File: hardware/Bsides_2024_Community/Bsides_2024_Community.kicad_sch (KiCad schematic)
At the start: 44 parts, among them J1 Add_On, J2 Battery, J3 Battery, J4 OLED, J5 Conn_01x05, J6 Conn_01x05, P1 USB_C_Plug_USB2.0, Q1 DMG3415U-7, SW1 ON, SW2 RESET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

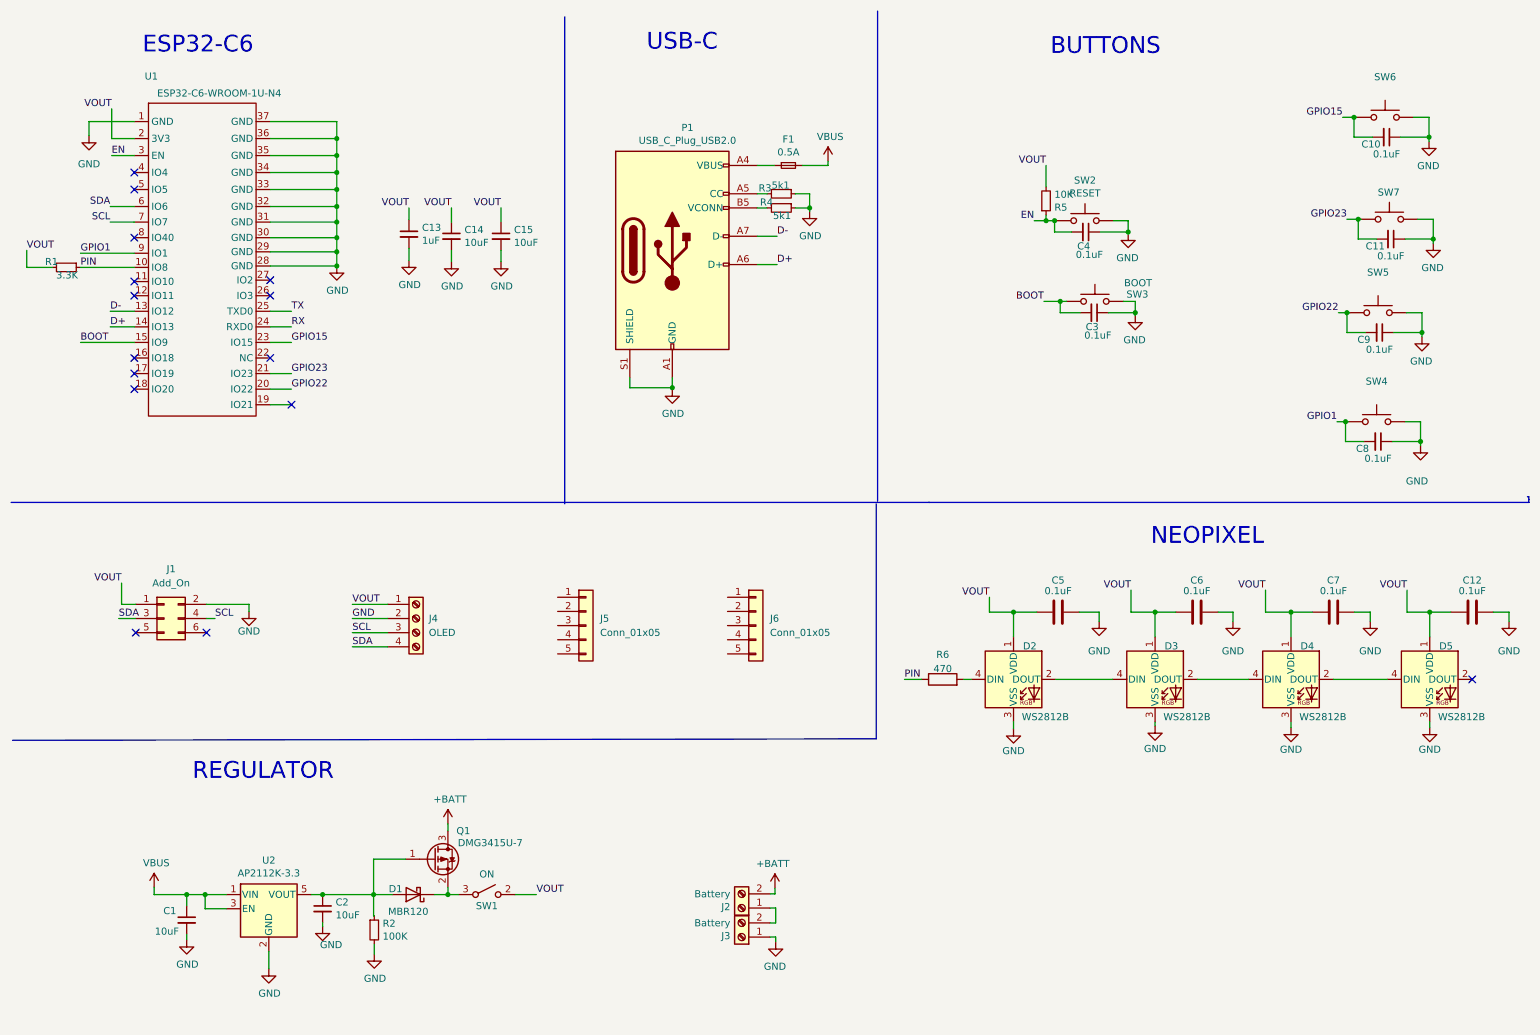
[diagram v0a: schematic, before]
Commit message: Revert "Merge branch 'main' of https://github.com/ElectronicCats/badge-bsides-cdmx-2024"
This reverts commit 844f9cf1141b02d246949023f3a5d84c3d1d6870, reversing
changes made to df45190e2e7c4c17babbd6f5b24a18277498f0c6.
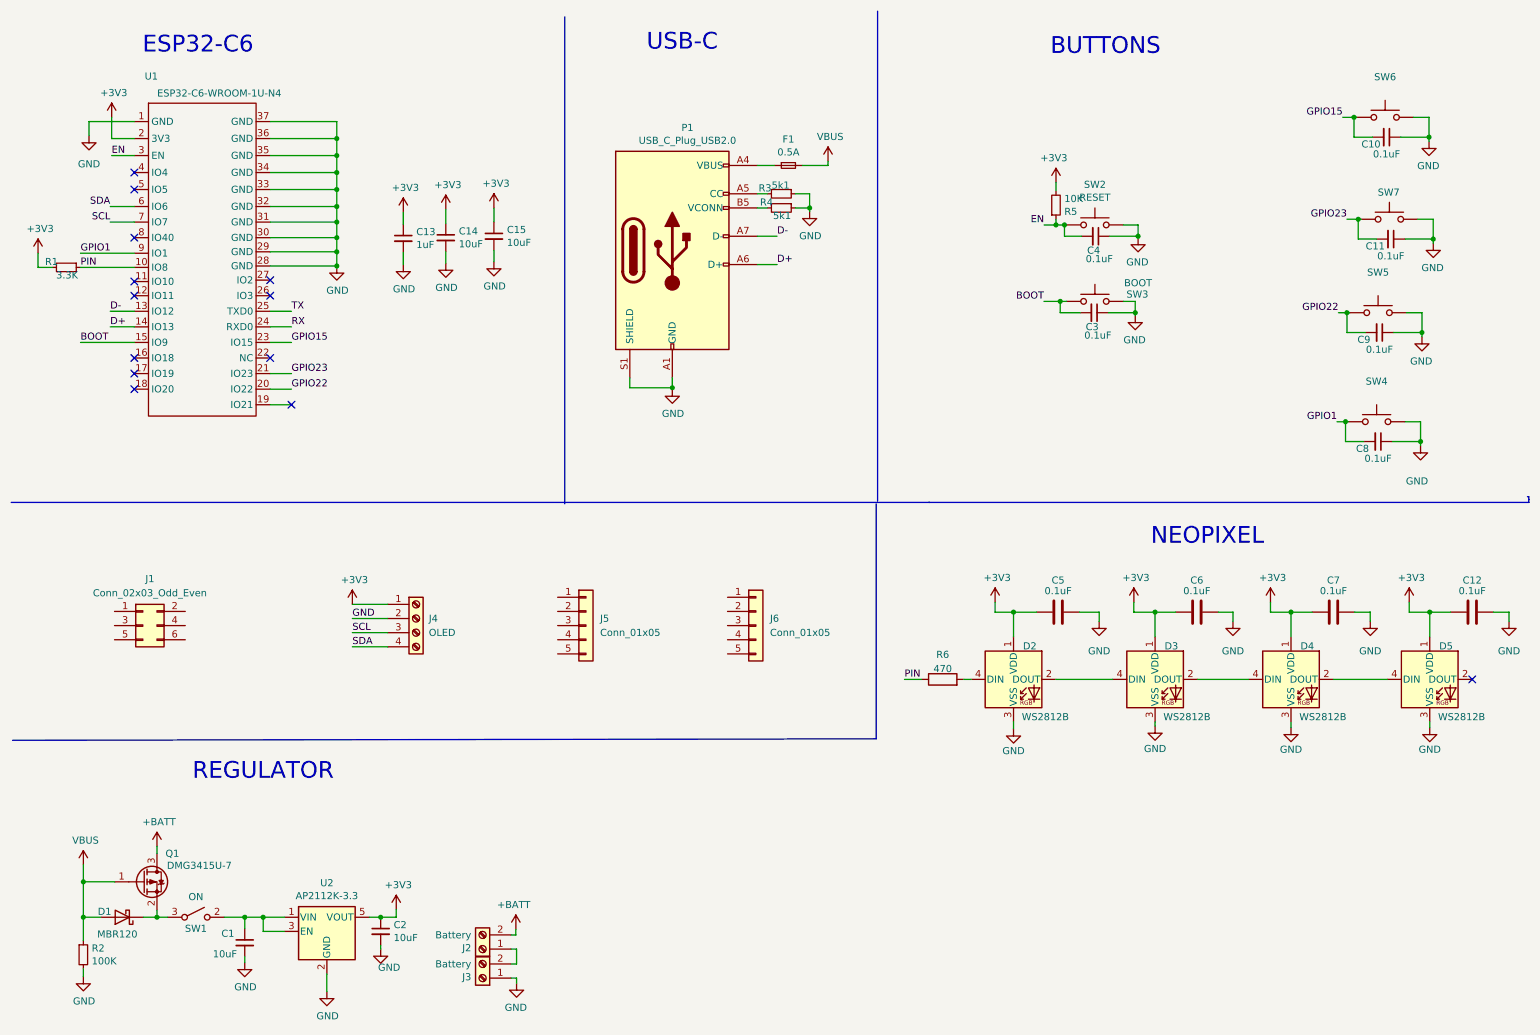
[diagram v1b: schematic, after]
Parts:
- J1: value Add_On -> Conn_02x03_Odd_Even
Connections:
- net GND: no longer J1.2 (Pin_2)
- net SCL: no longer J1.4 (Pin_4)
- net SDA: no longer J1.3 (Pin_3)
- net VBUS: now also D1.2 (A), Q1.1 (G), R2.1; no longer C1.1, U2.1 (VIN), U2.3 (EN)
- net VOUT renamed +3V3
- net +3V3: now also C2.1, U2.5 (VOUT); no longer J1.1 (Pin_1), SW1.2 (B)
- new net: C1.1, SW1.2 (B), U2.1 (VIN), U2.3 (EN)
- no-connect marks 15 -> 13
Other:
- moved on the sheet: C1, C13, C14, C15, C2, C4, D1, J2, J3, Q1, R2, R5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
